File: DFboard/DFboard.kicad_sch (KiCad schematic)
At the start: 4 parts, among them J1 DB25_Plug_MountingHoles_Male, J13 110-43-648-41-001000, J2 DB25_Receptacle_MountingHoles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, U1 Power

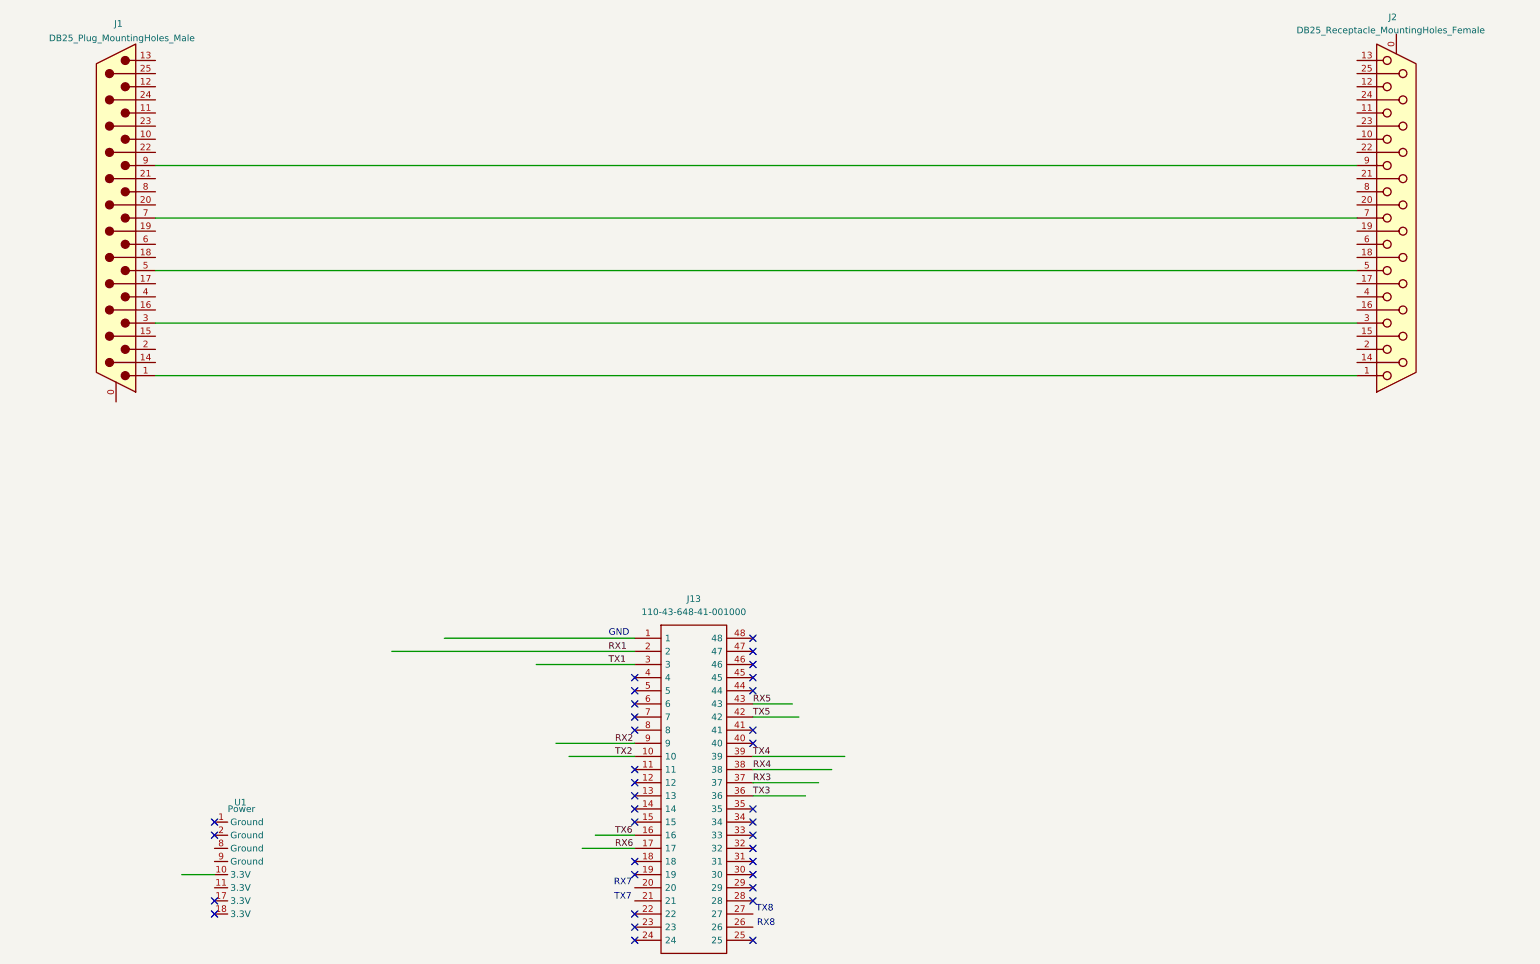
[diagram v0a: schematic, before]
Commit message: Updated MAX3232 Symbol.  Started adding jumpers
I need to verify which channel I should skip (Endstation).
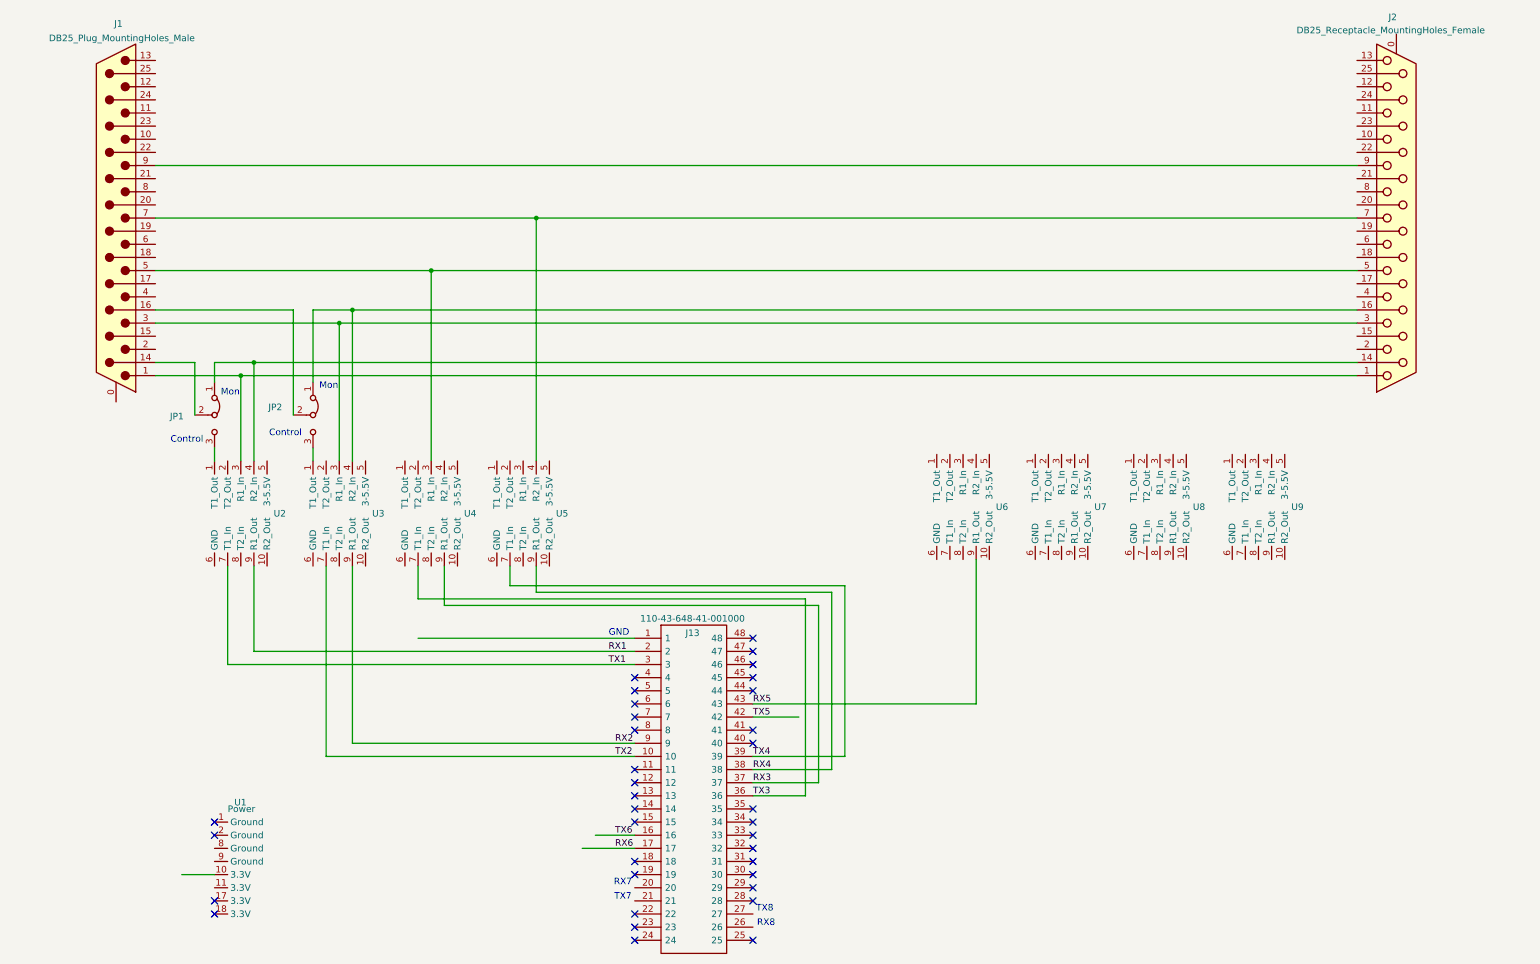
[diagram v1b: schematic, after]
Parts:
- added JP1: Jumper3, symbol Jumper:Jumper_3_Bridged12
- added JP2: Jumper_3_Bridged12, symbol Jumper:Jumper_3_Bridged12
- added U2, U3, U4, U5, U6, U7, U8, U9: ~, Misc:Max3232, symbol Misc:MAX3232
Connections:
- net RX1: now also U2.9 (R1_Out)
- net RX2: now also U3.9 (R1_Out)
- net RX3: now also U4.9 (R1_Out)
- net RX4: now also U5.9 (R1_Out)
- net RX5: now also U6.9 (R1_Out)
- net TX1: now also U2.7 (T1_In)
- net TX2: now also U3.7 (T1_In)
- net TX3: now also U4.7 (T1_In)
- net TX4: now also U5.7 (T1_In)
- net at J1.1, J2.1: now also U2.3 (R1_In)
- net at J1.14 (P14): now also JP1.2 (C)
- net at J1.16 (P16): now also JP2.2 (C)
- net at J1.3, J2.3: now also U3.3 (R1_In)
- net at J1.5, J2.5: now also U4.3 (R1_In)
- net at J1.7, J2.7: now also U5.4 (R2_In)
- net at J2.14 (P14): now also JP1.1 (A), U2.4 (R2_In)
- net at J2.16 (P16): now also JP2.1 (A), U3.4 (R2_In)
- new net: JP1.3 (B), U2.1 (T1_Out)
- new net: JP2.3 (B), U3.1 (T1_Out)
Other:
- note added: "Control"
- note added: "Mon"
